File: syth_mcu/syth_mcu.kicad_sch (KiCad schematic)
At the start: 40 parts, among them J1 Conn_01x05, J10 Conn_01x20, J11 Conn_01x20, J2 Conn_01x05, J3 USB_C_Receptacle_PowerOnly_6P, J5 Conn_01x20, J6 Conn_01x20, J7 Conn_01x16, J8 Conn_01x08, SW1 SW_Push, SW2 SW_Push, SW3 SW_Push, SW4 SW_Push, SW5 SW_Push, SW6 SW_Push, U2 YAAJ_WeAct_BlackPill_Part_Like, U3 AMS1117-3.3, U4 AMS1117-3.3, U5 TFT_320x240

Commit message: kicad: update pcb/sch/wrl
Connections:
- net C0: now also J7.1 (Pin_1); no longer J7.16 (Pin_16)
- net C1: now also J7.2 (Pin_2); no longer J7.15 (Pin_15)
- net C10: now also J7.11 (Pin_11); no longer J7.6 (Pin_6)
- net C11: now also J7.12 (Pin_12); no longer J7.5 (Pin_5)
- net C12: now also J7.13 (Pin_13); no longer J7.4 (Pin_4)
- net C13: now also J7.14 (Pin_14); no longer J7.3 (Pin_3)
- net C14: now also J7.15 (Pin_15); no longer J7.2 (Pin_2)
- net C15: now also J7.16 (Pin_16); no longer J7.1 (Pin_1)
- net C2: now also J7.3 (Pin_3); no longer J7.14 (Pin_14)
- net C3: now also J7.4 (Pin_4); no longer J7.13 (Pin_13)
- net C4: now also J7.5 (Pin_5); no longer J7.12 (Pin_12)
- net C5: now also J7.6 (Pin_6); no longer J7.11 (Pin_11)
- net C6: now also J7.7 (Pin_7); no longer J7.10 (Pin_10)
- net C7: now also J7.8 (Pin_8); no longer J7.9 (Pin_9)
- net C8: now also J7.9 (Pin_9); no longer J7.8 (Pin_8)
- net C9: now also J7.10 (Pin_10); no longer J7.7 (Pin_7)
- net PA5: now also J8.5 (Pin_5)
- net PA6: now also J8.4 (Pin_4)
- net PA7: now also J8.3 (Pin_3)
- net PB1: no longer J8.4 (Pin_4)
- net PB10: no longer J8.5 (Pin_5)
- net PB2: no longer J8.3 (Pin_3)
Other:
- moved on the sheet: J7

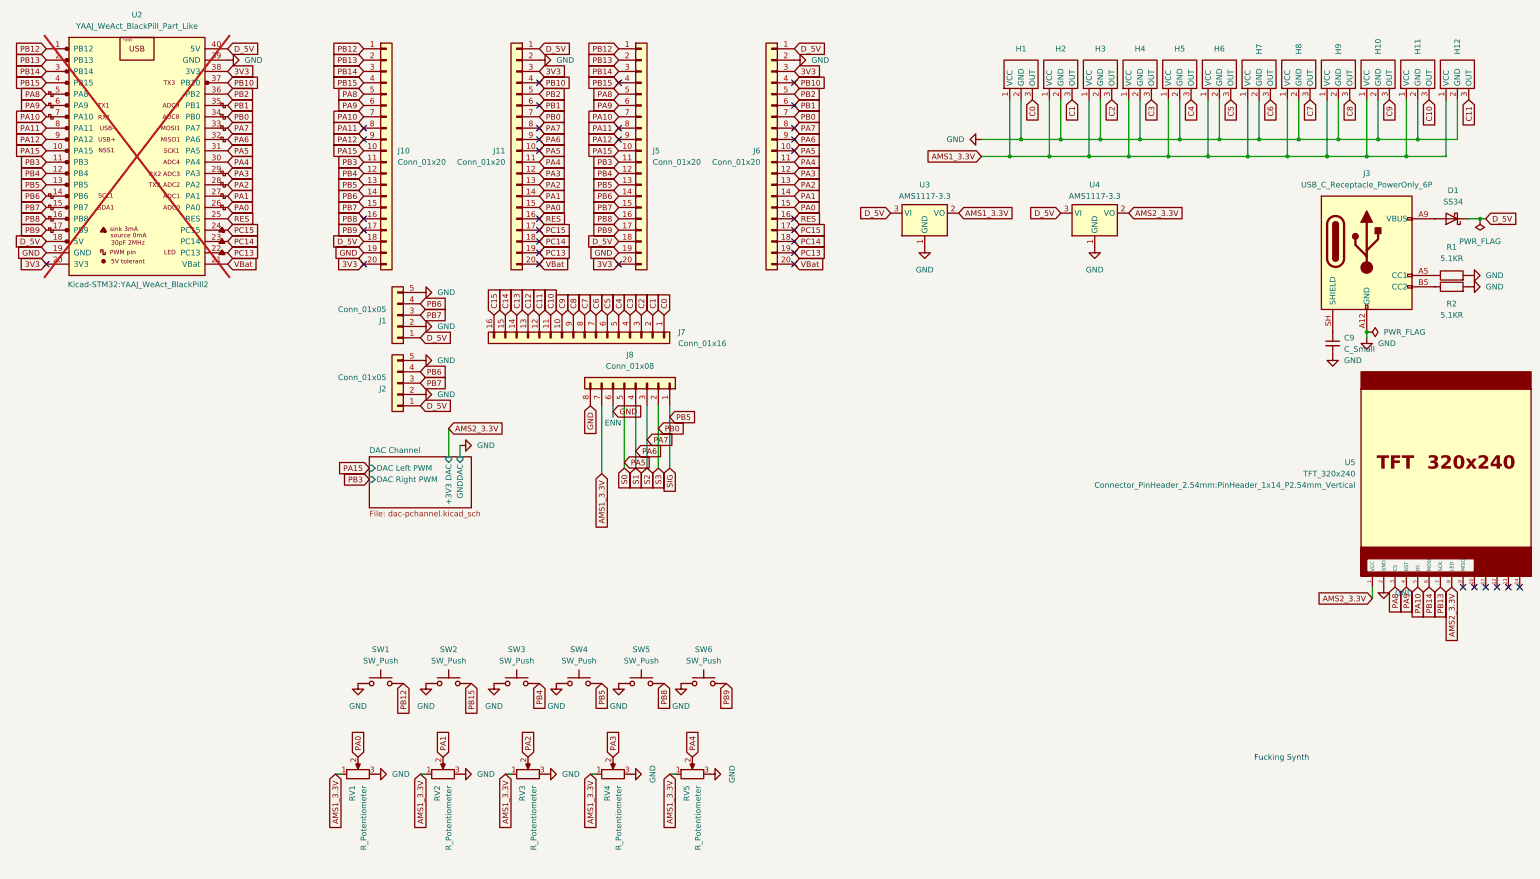
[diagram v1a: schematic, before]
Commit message: Power, comm and hall sensors routings
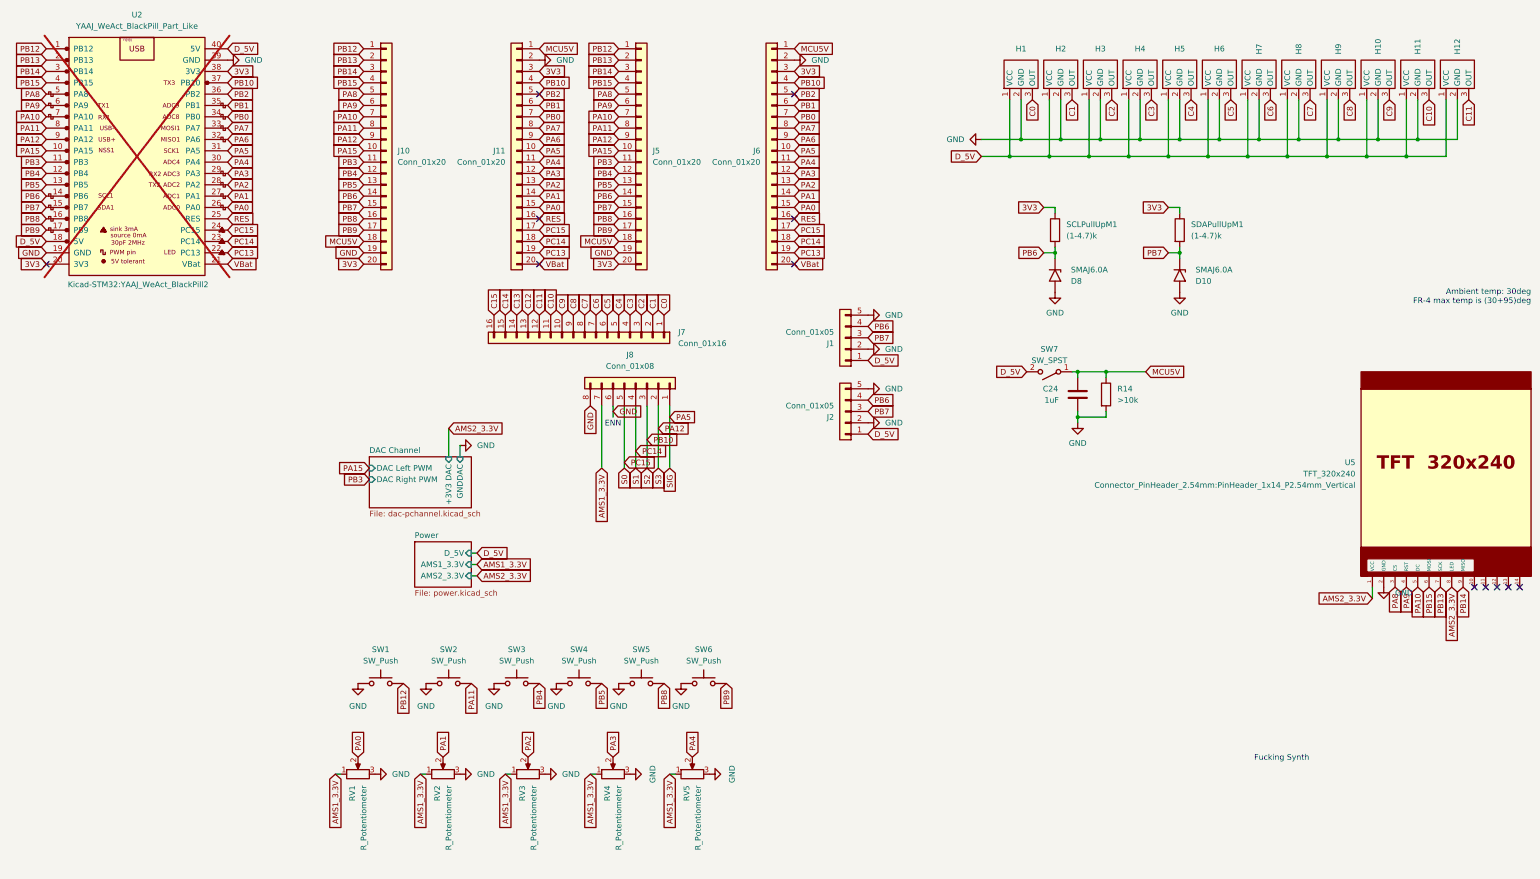
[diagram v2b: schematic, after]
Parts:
- removed C9: C_Small, Capacitor_THT:C_Disc_D5.0mm_W2.5mm_P2.50mm, symbol Device:C_Small
- removed D1: SS34, Diode_SMD:D_SMA, symbol Diode:SS14
- removed J3: USB_C_Receptacle_PowerOnly_6P, Connector_USB:USB_C_Receptacle_Amphenol_12401610E4-2A, symbol Connector:USB_C_Receptacle_PowerOnly_6P
- removed R1, R2: 5.1KR, Resistor_THT:R_Axial_DIN0207_L6.3mm_D2.5mm_P10.16mm_Horizontal, symbol Device:R
- removed U3, U4: AMS1117-3.3, Package_TO_SOT_SMD:SOT-223-3_TabPin2, symbol Regulator_Linear:AMS1117-3.3
- added C24: 1uF, Capacitor_THT:C_Disc_D5.0mm_W2.5mm_P5.00mm, symbol Device:C
- added D10, D8: SMAJ6.0A, Diode_SMD:D_SMA, symbol Diode:SMAJ5.0A
- added R14: >10k, Resistor_THT:R_Axial_DIN0207_L6.3mm_D2.5mm_P10.16mm_Horizontal, symbol Device:R
- added SCLPullUpM1, SDAPullUpM1: (1-4.7)k, Resistor_THT:R_Axial_DIN0207_L6.3mm_D2.5mm_P10.16mm_Horizontal, symbol Device:R
- added SW7: SW_SPST, symbol Switch:SW_SPST
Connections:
- net 3V3: now also SCLPullUpM1.1, SDAPullUpM1.1
- net AMS1_3.3V: no longer H1.1 (VCC), H10.1 (VCC), H11.1 (VCC), H12.1 (VCC), H2.1 (VCC), H3.1 (VCC), H4.1 (VCC), H5.1 (VCC), H6.1 (VCC), H7.1 (VCC), H8.1 (VCC), H9.1 (VCC)
- net D_5V: now also H1.1 (VCC), H10.1 (VCC), H11.1 (VCC), H12.1 (VCC), H2.1 (VCC), H3.1 (VCC), H4.1 (VCC), H5.1 (VCC), H6.1 (VCC), H7.1 (VCC), H8.1 (VCC), H9.1 (VCC), SW7.2 (B); no longer J10.18 (Pin_18), J11.1 (Pin_1), J5.18 (Pin_18), J6.1 (Pin_1)
- net GND: now also C24.2, D10.2 (A2), D8.2 (A2), R14.2
- net PA11: now also SW2.2
- net PA12: now also J8.2 (Pin_2)
- net PA5: now also J8.1 (Pin_1); no longer J8.5 (Pin_5)
- net PA6: no longer J8.4 (Pin_4)
- net PA7: no longer J8.3 (Pin_3)
- net PB0: no longer J8.2 (Pin_2)
- net PB10: now also J8.3 (Pin_3)
- net PB14: now also U5.9 (MISO); no longer U5.6 (MOSI)
- net PB15: now also U5.6 (MOSI); no longer SW2.2
- net PB5: no longer J8.1 (Pin_1)
- net PB6: now also D8.1 (A1), SCLPullUpM1.2
- net PB7: now also D10.1 (A1), SDAPullUpM1.2
- net PC14: now also J8.4 (Pin_4)
- net PC15: now also J8.5 (Pin_5)
- new net MCU5V: C24.1, J10.18 (Pin_18), J11.1 (Pin_1), J5.18 (Pin_18), J6.1 (Pin_1), R14.1, SW7.1 (A)
- no-connect marks 36 -> 12
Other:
- added sheet Power (power.kicad_sch)
- note added: "Ambient temp: 30deg FR-4 max temp is (30+95)deg"
- moved on the sheet: J1, J2

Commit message: All traces, no drc runs yet
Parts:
- added D11, D9: SMAJ6.0A, Diode_SMD:D_SMA, symbol Diode:SMAJ5.0A
- SW7: footprint (none) -> synth:SS12D10
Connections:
- net GND: now also D11.2 (A2), D9.2 (A2)
- net PB6: now also D9.1 (A1)
- net PB7: now also D11.1 (A1)
- net PC14: now also J8.5 (Pin_5); no longer J8.4 (Pin_4)
- net PC15: now also J8.4 (Pin_4); no longer J8.5 (Pin_5)
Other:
- moved on the sheet: D10, SDAPullUpM1

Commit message: pcb: cream bun review fixes (J7 position, Sim.Pins, reformat)
- J7 (1x16 MUX channel socket) moved -2.54mm in x: 154.35->151.81
  (aligns mux channels to hall sensor row)
- dac-pchannel: Sim.Pins corrected on Q1-Q4 + embedded lib defs
  SI2307DS/SI2304DS actual SOT-23 pinout: 1=G 2=S 3=D
  (was 1=D 2=G 3=S per Simulation_SPICE symbol default)
  NOTE: Sim.Pins is SPICE/documentation only — PCB pads still
  routed wrong. Full fix requires schematic symbol swap +
  PCB re-route (GUI work, see open items)
- PB7 I2C trace gap NOT fixed here — requires GUI routing
  (F.Cu gap at bbox 182.26,122.67 -> 191.53,130.30)
- Remaining changes: KiCad auto-reformat from last GUI open

Claude-Session: https://claude.ai/code/session_01VrAYoAfZXAEYgerctdkqLT
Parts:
- SW1, SW2, SW3, SW4, SW5, SW6: footprint synth:MX-Alps-Choc-1U -> Switch_Keyboard_Hotswap_Kailh:SW_Hotswap_Kailh_Choc_V1_1.00u
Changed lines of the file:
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@@
 			)
 		)
-		(property "Footprint" "synth:MX-Alps-Choc-1U"
+		(property "Footprint" "Switch_Keyboard_Hotswap_Kailh:SW_Hotswap_Kailh_Choc_V1_1.00u"
 			(at 97.79 152.4 0)
 			(hide yes)
@@
 			)
 		)
-		(property "Footprint" "synth:MX-Alps-Choc-1U"
+		(property "Footprint" "Switch_Keyboard_Hotswap_Kailh:SW_Hotswap_Kailh_Choc_V1_1.00u"
 			(at 40.64 152.4 0)
 			(hide yes)
@@
 			)
 		)
-		(property "Footprint" "synth:MX-Alps-Choc-1U"
+		(property "Footprint" "Switch_Keyboard_Hotswap_Kailh:SW_Hotswap_Kailh_Choc_V1_1.00u"
 			(at 69.85 152.4 0)
 			(hide yes)
@@
 			)
 		)
-		(property "Footprint" "synth:MX-Alps-Choc-1U"
+		(property "Footprint" "Switch_Keyboard_Hotswap_Kailh:SW_Hotswap_Kailh_Choc_V1_1.00u"
 			(at 25.4 152.4 0)
 			(hide yes)
@@
 			)
 		)
-		(property "Footprint" "synth:MX-Alps-Choc-1U"
+		(property "Footprint" "Switch_Keyboard_Hotswap_Kailh:SW_Hotswap_Kailh_Choc_V1_1.00u"
 			(at 55.88 152.4 0)
 			(hide yes)
@@
 			)
 		)
-		(property "Footprint" "synth:MX-Alps-Choc-1U"
+		(property "Footprint" "Switch_Keyboard_Hotswap_Kailh:SW_Hotswap_Kailh_Choc_V1_1.00u"
 			(at 83.82 152.4 0)
 			(hide yes)

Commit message: Fixes from review 2
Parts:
- U5: footprint Connector_PinHeader_2.54mm:PinHeader_1x14_P2.54mm_Vertical -> Connector_PinSocket_2.54mm:PinSocket_1x14_P2.54mm_Vertical
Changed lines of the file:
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@@
 			)
 		)
-		(property "Footprint" "Connector_PinHeader_2.54mm:PinHeader_1x14_P2.54mm_Vertical"
+		(property "Footprint" "Connector_PinSocket_2.54mm:PinSocket_1x14_P2.54mm_Vertical"
 			(at 243.84 113.0299 0)
 			(show_name no)

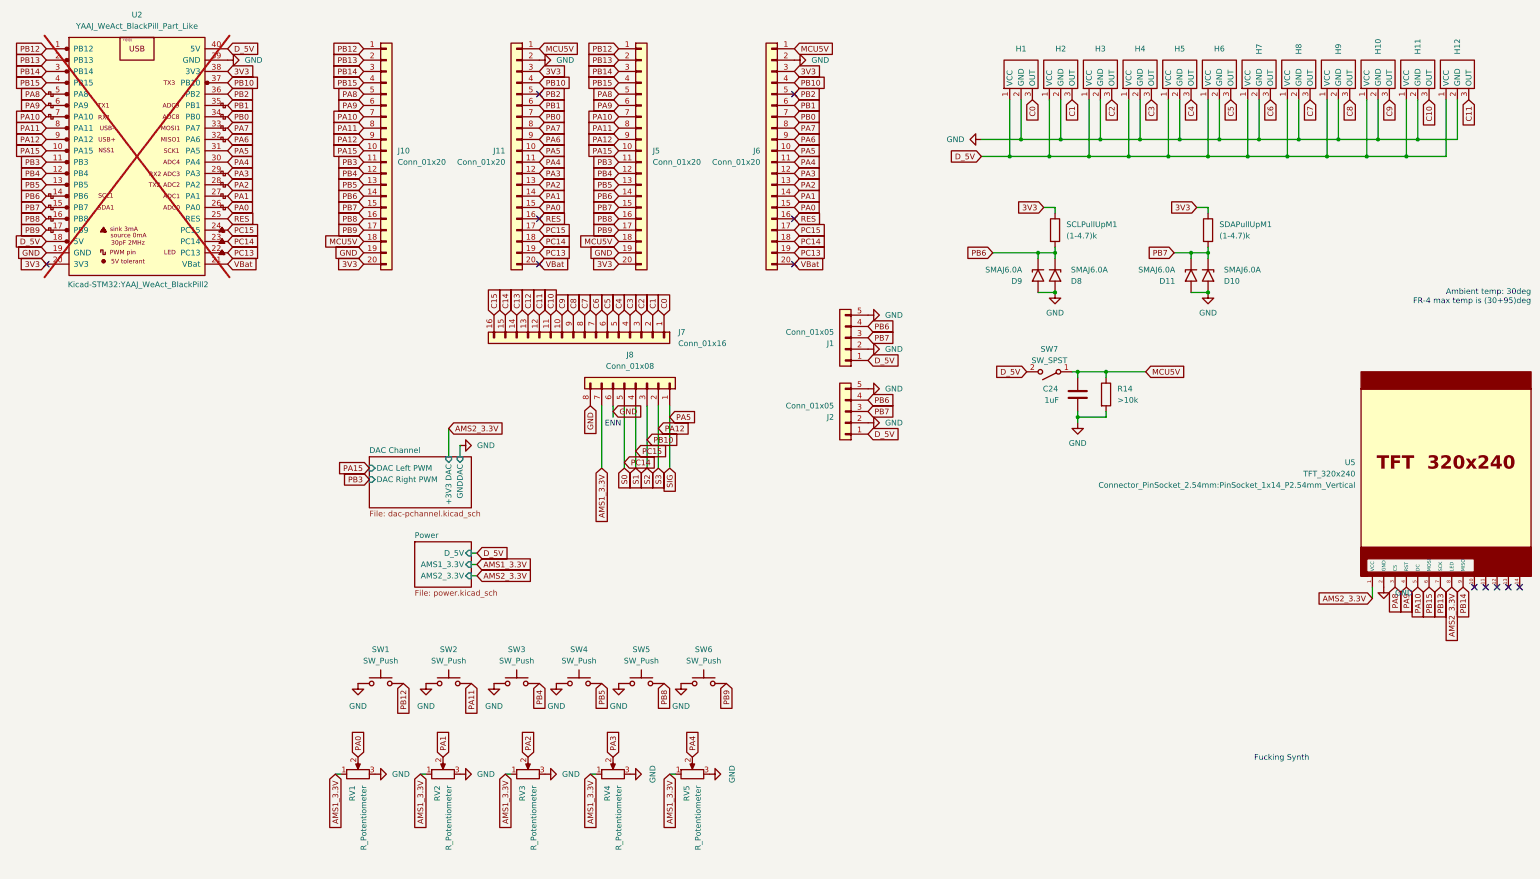
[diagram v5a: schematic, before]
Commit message: Unity-gain audio, merge AMS, 12 pots to mux, revs, footprint
Footprints:
- RXEF fuses with 1x dimension silkscreen and +0.2mm courtyard
- AMS1117 with 0.5mm minimum soldering space on all sides
- SS12D10 wider pins and add courtyard
- Changed orientation of AH3503 TO-92 to match datasheet
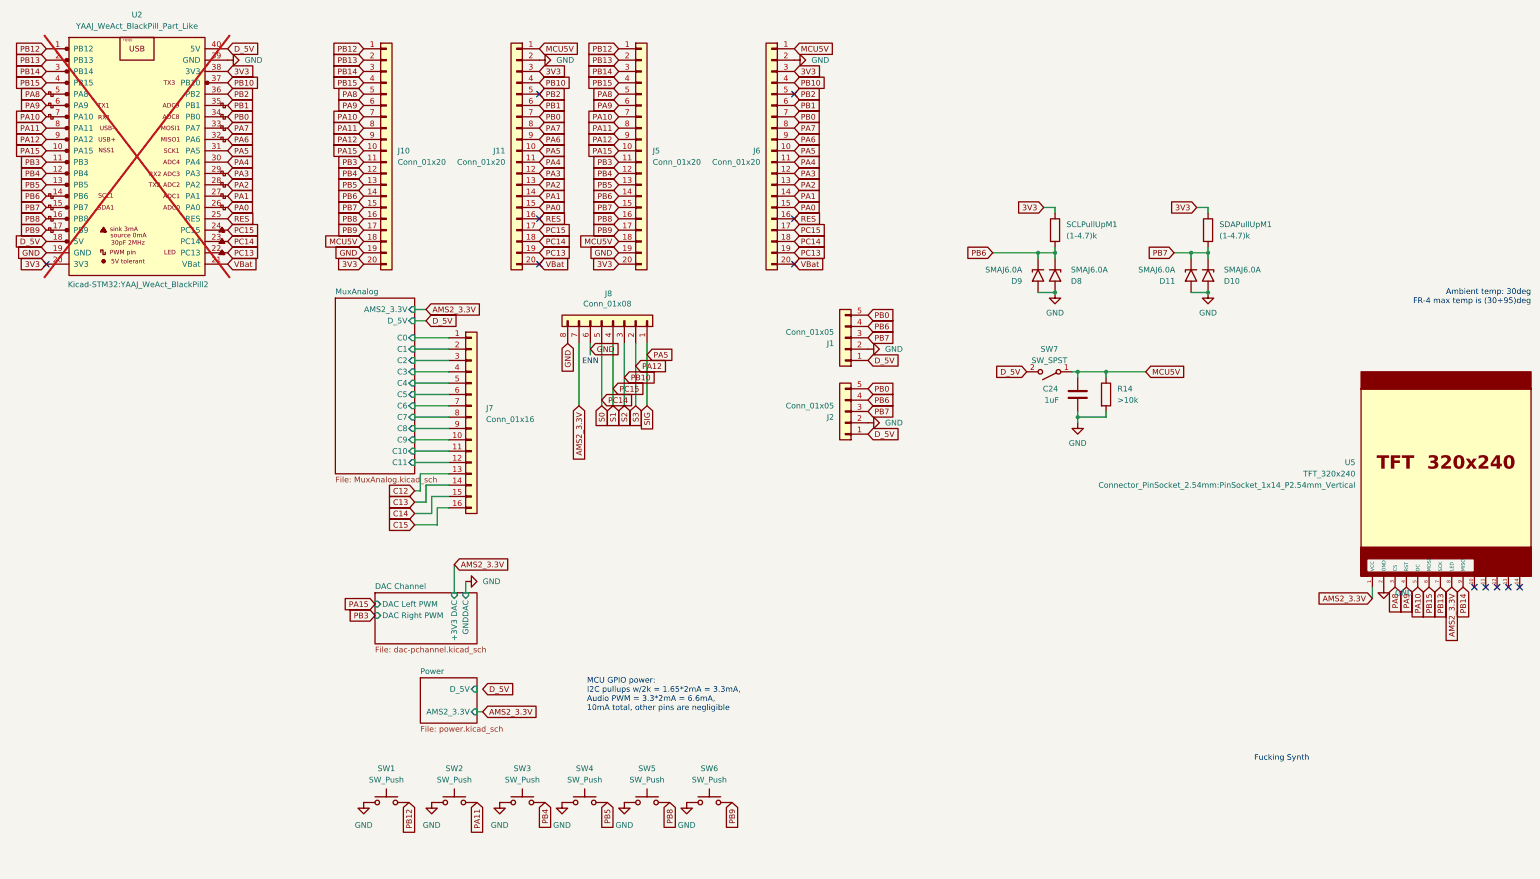
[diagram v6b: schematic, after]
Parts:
- removed H1, H10, H11, H12, H2, H3, H4, H5, H6, H7, H8, H9: (no value), Package_TO_SOT_THT:TO-92_Inline, symbol synth:H3503
- removed RV1, RV2, RV3, RV4, RV5: R_Potentiometer, synth:Potentiometer_Alps_RK09K_Single_Vertical, symbol Device:R_Potentiometer
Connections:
- net AMS1_3.3V is gone; now on net AMS2_3.3V: J8.7 (Pin_7)
- net GND: no longer J1.5 (Pin_5), J2.5 (Pin_5)
- net PB0: now also J1.5 (Pin_5), J2.5 (Pin_5)
- net C0 renamed MuxAnalog/C0
- net C1 renamed MuxAnalog/C1
- net C10 renamed MuxAnalog/C10
- net C11 renamed MuxAnalog/C11
- net C2 renamed MuxAnalog/C2
- net C3 renamed MuxAnalog/C3
- net C4 renamed MuxAnalog/C4
- net C5 renamed MuxAnalog/C5
- net C6 renamed MuxAnalog/C6
- net C7 renamed MuxAnalog/C7
- net C8 renamed MuxAnalog/C8
- net C9 renamed MuxAnalog/C9
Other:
- added sheet MuxAnalog (MuxAnalog.kicad_sch)
- sheet Power ports: added none; removed AMS1_3.3V
- note added: "MCU GPIO power: I2C pullups w/2k = 1.65*2mA = 3.3mA, Audio PWM = 3.3*2mA = 6.6mA, 10mA total, other pins are negligible"
- moved on the sheet: J7, J8, SW1, SW2, SW3, SW4, SW5, SW6
